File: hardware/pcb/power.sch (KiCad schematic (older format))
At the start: 6 parts

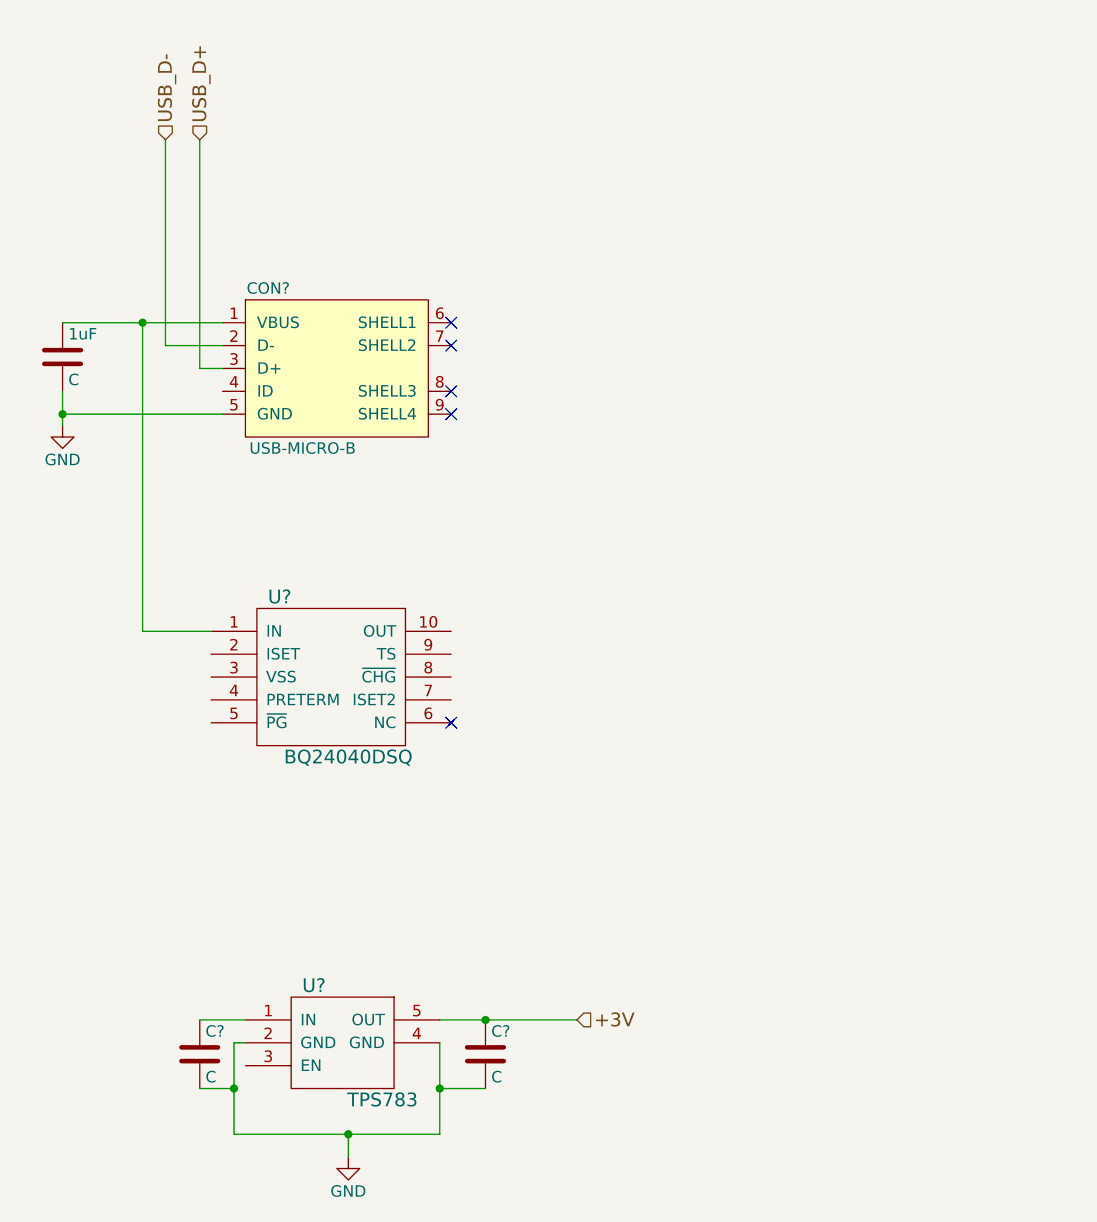
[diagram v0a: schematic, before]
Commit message: More work on power section
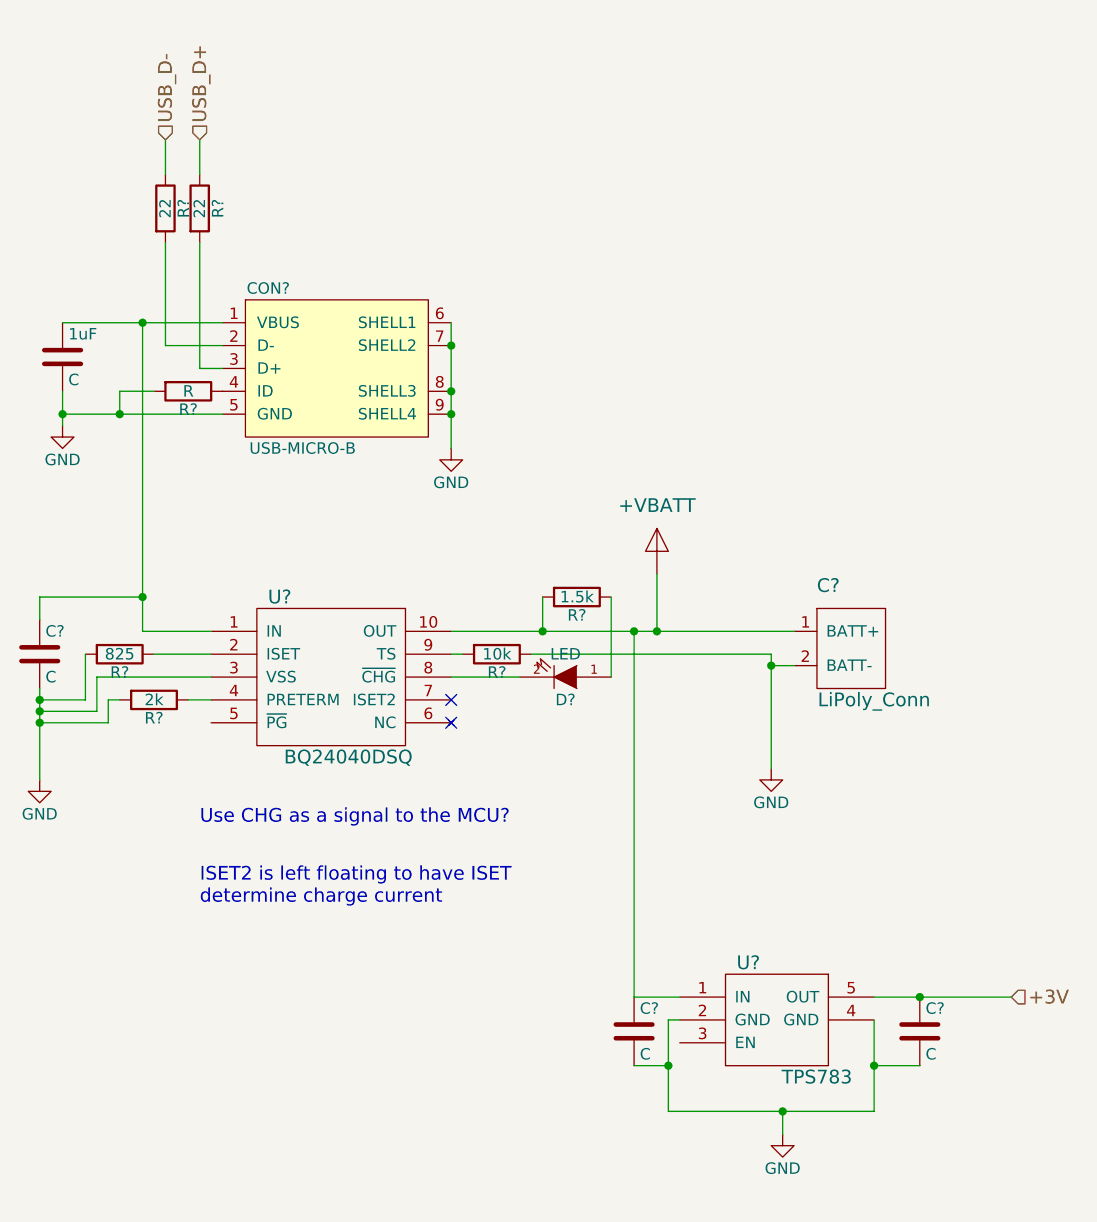
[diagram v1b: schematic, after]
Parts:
- added C?: C, symbol C
- added C?: LiPoly_Conn, symbol LiPoly_Conn
- added D?: LED, symbol LED
- added P?: +VBATT, symbol +VBATT
- added R? (x2): 22, symbol R
- added R?: R, symbol R
- added R?: 825, symbol R
- added R?: 2k, symbol R
- added R?: 10k, symbol R
- added R?: 1.5k, symbol R
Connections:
- net GND: now also CON?.6 (SHELL1), CON?.7 (SHELL2), CON?.8 (SHELL3), CON?.9 (SHELL4), U?.3 (VSS), C?.2, C?.2 (BATT-), R?.1, R?.2, R?.2, R?.2
- net USB_D+: now also R?.1; no longer CON?.3 (D+)
- net USB_D-: now also R?.1; no longer CON?.2 (D-)
- net at 1uF.1, CON?.1 (VBUS), U?.1 (IN): now also C?.1
- net at CON?.4 (ID): now also R?.1
- net Vbatt: now reaches U?.10 (OUT)
- net Vbatt: now also C?.1, U?.1 (IN), C?.1 (BATT+), P?.1 (Vbatt), R?.2
- net at U?.2 (ISET): now also R?.1
- net at U?.4 (PRETERM): now also R?.1
- net at U?.8 (~CHG): now also D?.2 (K)
- net at U?.9 (TS): now also R?.2
- new net: CON?.2 (D-), R?.2
- new net: CON?.3 (D+), R?.2
- new net: D?.1 (A), R?.1
- no-connect marks 5 -> 2
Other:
- note added: "ISET2 is left floating to have ISET \ndetermine charge current\n"
- note added: "Use CHG as a signal to the MCU?"
- moved on the sheet: C?, U?

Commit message: added sensor connections
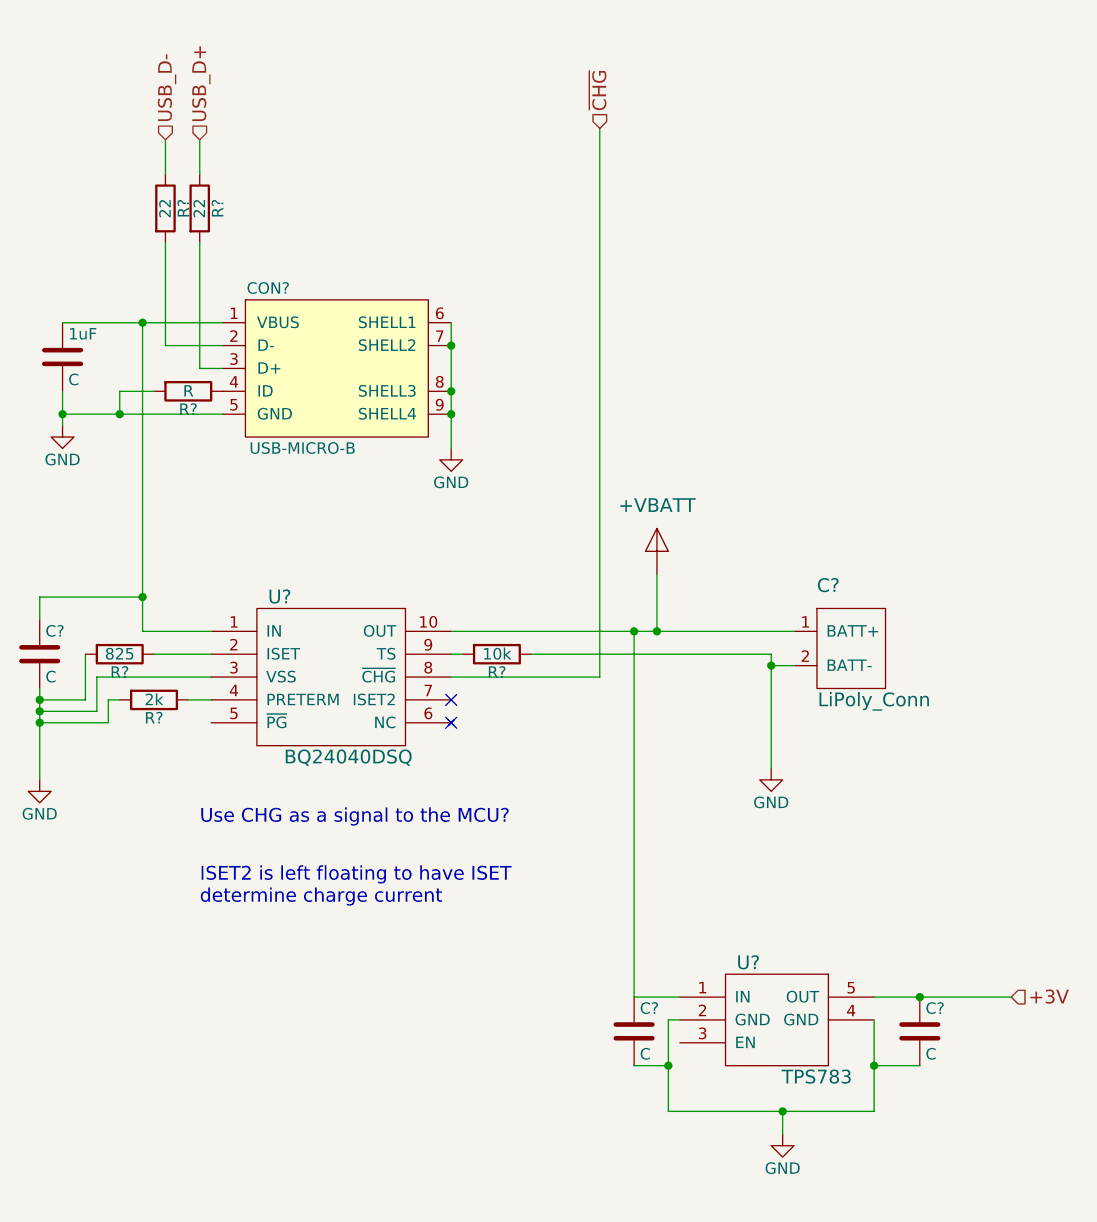
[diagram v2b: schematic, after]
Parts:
- removed D?: LED, symbol LED
- removed R?: 1.5k, symbol R
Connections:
- net ~CHG: now reaches U?.8 (~CHG)
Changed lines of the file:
@@
 	4850 5600 4850 4000
 Connection ~ 4850 4000
-$Comp
-L LED D?
-U 1 1 5530138B
-P 4550 4200
-F 0 "D?" H 4550 4300 50  0000 C CNN
-F 1 "LED" H 4550 4100 50  0000 C CNN
-F 2 "" H 4550 4200 60  0000 C CNN
-F 3 "" H 4550 4200 60  0000 C CNN
-	1    4550 4200
-	-1   0    0    1
-$EndComp
-$Comp
-L R R?
-U 1 1 5530144D
-P 4600 3850
-F 0 "R?" V 4680 3850 50  0000 C CNN
-F 1 "1.5k" V 4600 3850 50  0000 C CNN
-F 2 "" V 4530 3850 30  0000 C CNN
-F 3 "" H 4600 3850 30  0000 C CNN
-	1    4600 3850
-	0    1    1    0
-$EndComp
-Wire Wire Line
-	4450 3850 4450 4000
-Connection ~ 4450 4000
-Wire Wire Line
-	4750 3850 4750 4200
-Wire Wire Line
-	4350 4200 4050 4200
 Text Notes 2950 4850 0    60   ~ 0
 Use CHG as a signal to the MCU?
@@
 Text Notes 2950 5200 0    60   ~ 0
 ISET2 is left floating to have ISET \ndetermine charge current\n
+Text HLabel 4700 1800 1    60   Input ~ 0
+~CHG
+Wire Wire Line
+	4050 4200 4700 4200
+Wire Wire Line
+	4700 4200 4700 1800
 $EndSCHEMATC
